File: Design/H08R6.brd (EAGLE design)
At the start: 34.6 x 30 mm, 41 parts, among them P1 HEXABIT_17.32, U1 STM32G0B1CEU6N, U2 VL53L8CXV0GC_1, U3 LDK130PU18R, U4 TCK107AG,LF, U5 PI4ULS3V204ZBEX, U6 PI4ULS3V204ZBEX, X1 XTALL_CSTCE8M00G52

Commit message: Correct the EN pin of the level shifter IC referencing.
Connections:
- net +1.8V: now also R11.2
- net VDD: no longer R11.2
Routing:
- net VDD: track 16.6 -> 12.8 mm, vias 33 -> 32
- net +1.8V: track 38.7 -> 42.0 mm
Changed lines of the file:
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@@
 <contactref element="C9" pad="1"/>
 <contactref element="C15" pad="1"/>
-<contactref element="R11" pad="2"/>
 <contactref element="P1" pad="PAD_PU7"/>
 <contactref element="P1" pad="PAD_PU8"/>
@@
 <via x="8.41375" y="14.9225" extent="1-16" drill="0.35" diameter="0.75"/>
 <via x="8.09625" y="14.12875" extent="1-16" drill="0.35" diameter="0.75"/>
-<wire x1="-3.33375" y1="21.2875" x2="-4.1425" y2="21.2875" width="0.254" layer="1"/>
-<wire x1="-5.23875" y1="23.66865" x2="-5.3975" y2="23.8274" width="0.254" layer="1"/>
-<wire x1="-5.23875" y1="23.66865" x2="-5.23875" y2="22.38375" width="0.254" layer="1"/>
-<via x="-5.3975" y="23.8274" extent="1-16" drill="0.25" diameter="0.55"/>
 <wire x1="-5.3975" y1="23.8274" x2="-5.3975" y2="23.23375" width="0.254" layer="16"/>
 <wire x1="-5.3975" y1="23.23375" x2="-5.35375" y2="23.19" width="0.254" layer="16"/>
-<wire x1="-4.1425" y1="21.2875" x2="-5.23875" y2="22.38375" width="0.254" layer="1"/>
 <polygon width="0.1524" layer="1" thermals="no">
 <vertex x="0.635" y="22.38375"/>
@@
 <wire x1="6.0325" y1="24.4475" x2="6.0062875" y2="24.4475" width="0.3048" layer="1"/>
 <wire x1="6.0062875" y1="24.4475" x2="5.4527" y2="23.8939125" width="0.3048" layer="1"/>
+<wire x1="-1.905" y1="23.495" x2="-5.35375" y2="23.19" width="0" layer="19" extent="16-16"/>
 </signal>
 <signal name="GND">
@@
 <wire x1="0" y1="18.57375" x2="-0.9525" y2="18.57375" width="0.4064" layer="1"/>
 <wire x1="-0.9525" y1="18.57375" x2="-1.11125" y2="18.415" width="0.4064" layer="1"/>
+<contactref element="R11" pad="2"/>
+<wire x1="-3.33375" y1="21.2875" x2="-3.33375" y2="24.13" width="0.3048" layer="1"/>
+<wire x1="-3.33375" y1="24.13" x2="-3.01625" y2="24.4475" width="0.3048" layer="1"/>
 </signal>
 <signal name="CONTROLLED_AVDD">

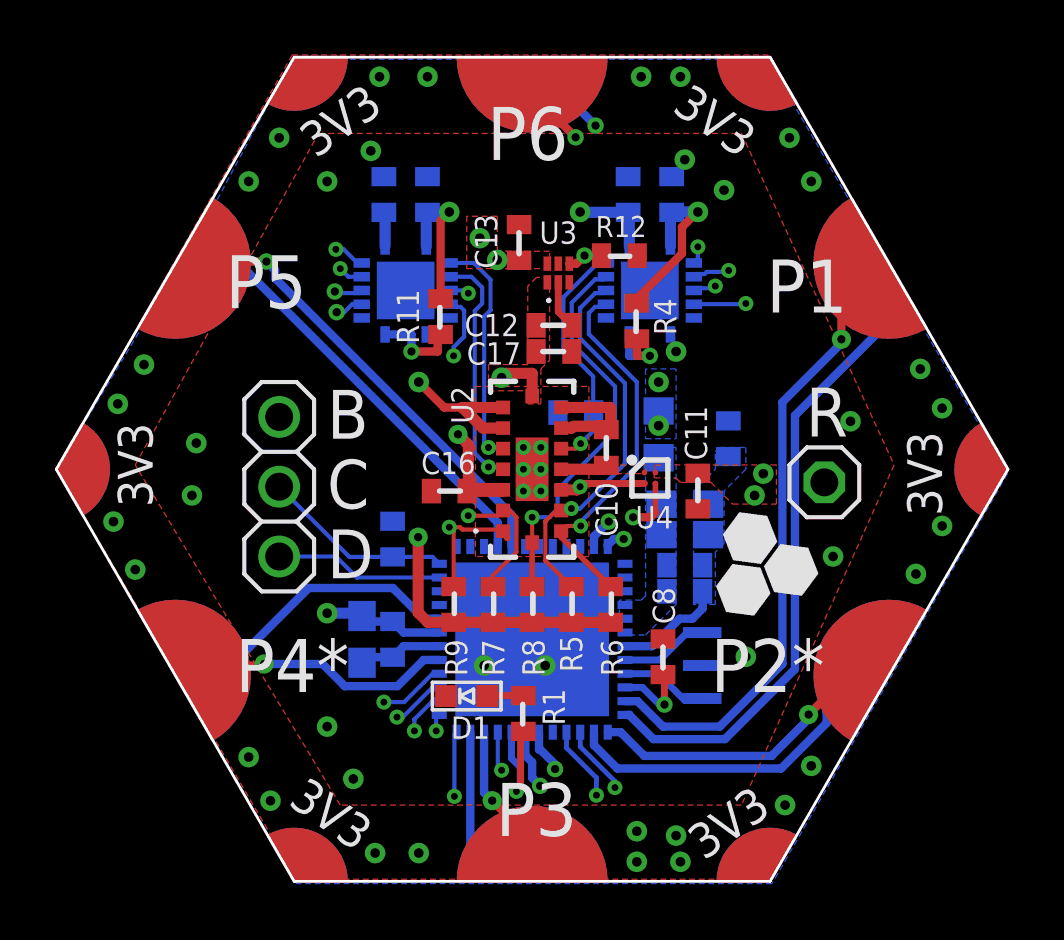
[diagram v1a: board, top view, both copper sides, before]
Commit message: -Fix missing connection -Add TVS -Update the logo -Fix clearence and soldermask
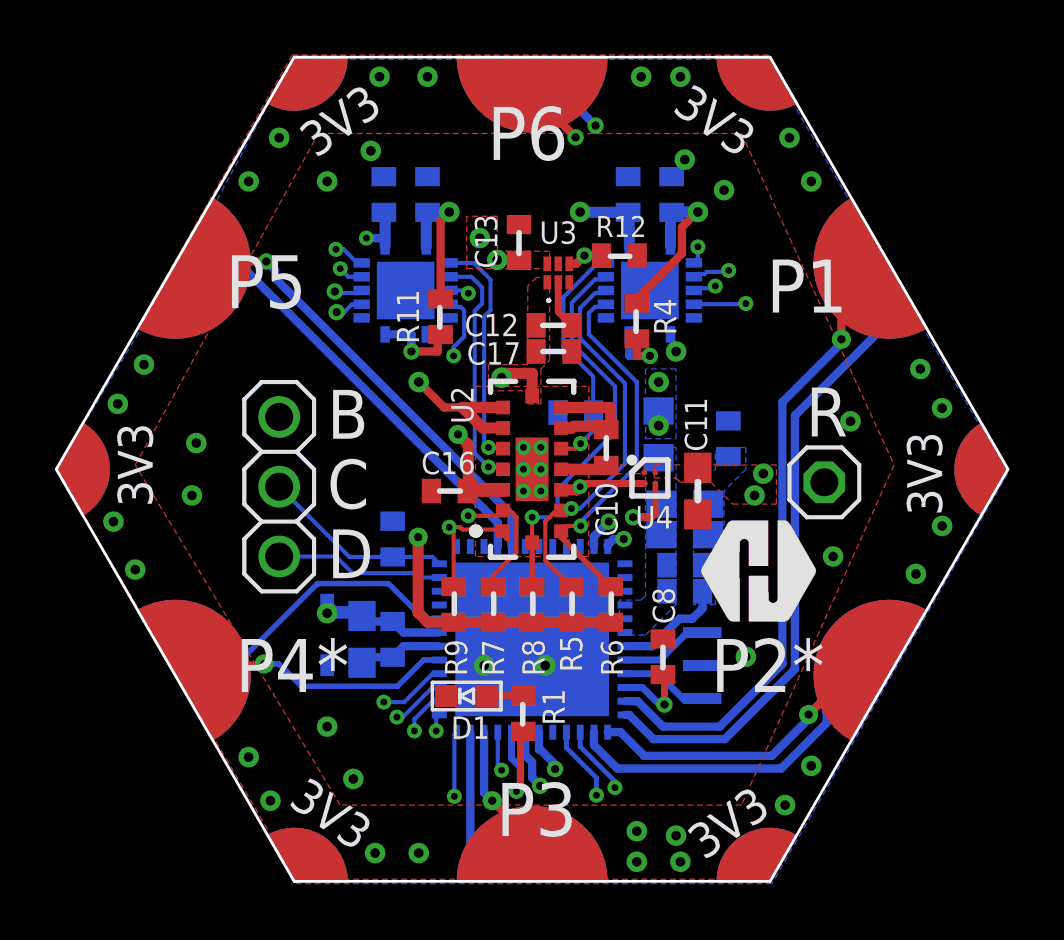
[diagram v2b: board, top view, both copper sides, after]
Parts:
- added D2: BOURNS_CDSOD323-T03SCBOURNS_CDSOD323-T03SC_0_0, HEXABITZ_RCLS:BOURNS_CDSOD323-T03SC_0
- added TRIMBLE-LOGO1: HEXA-LOGO, HEXABITZ_USER_INTERFACE_PARTS:HEXA-LOGO
- C11: device HEXABITZ_RCLS:C-0402 -> HEXABITZ_RCLS:C-0603
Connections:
- net GND: now also D2.2
- net VDD: now also D2.1
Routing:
- net VDD: track 12.8 -> 14.8 mm, vias 32 -> 33

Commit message: -Change the MCU footprint to STM32G0B1CEU6
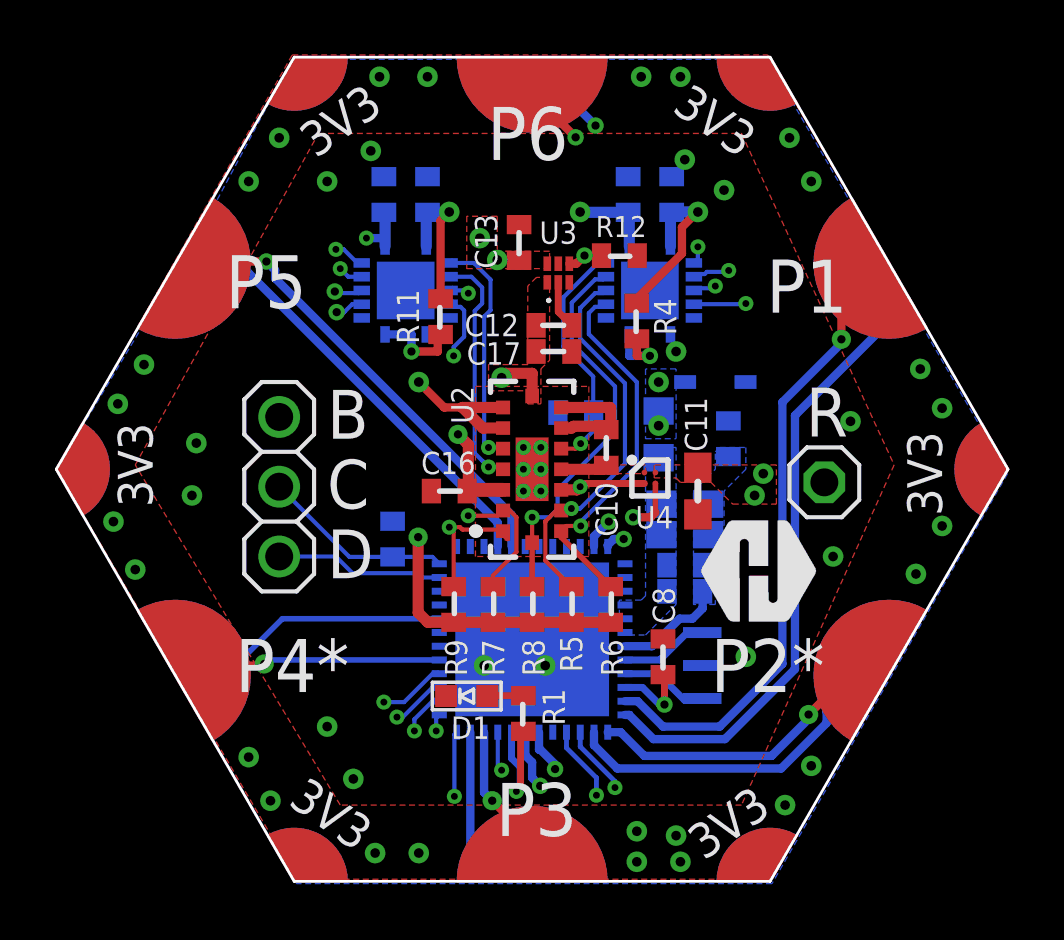
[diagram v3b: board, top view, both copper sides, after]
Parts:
- removed C3: 100nF, HEXABITZ_RCLS:C-0402
- removed C4: 4.7uF, HEXABITZ_RCLS:C-0603-POL
- U1: value STM32G0B1CEU6N -> STM32G0B1CEU6QFN_B1CEU6_STM-L; device HEXABITZ_ICs:HEXABITZ_ICS_QFN_B1CEU6_STM-L -> HEXABITZ_ICs:QFN_B1CEU6_STM-L
- moved D2 16.9 mm to (6.67, 18.3), turned to 180 degrees
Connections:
- net GND: no longer C3.2, C4.2, U1.30
- net VDD: no longer C3.1, C4.1, U1.31
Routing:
- net VDD: track 14.8 -> 9.03 mm, vias 33 -> 32
- net GND: track 18.6 -> 15.5 mm
- net USART1_RX: track 10.8 -> 9.72 mm
- net USART1_TX: track 9.77 -> 9.10 mm
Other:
- board text added: "*"
